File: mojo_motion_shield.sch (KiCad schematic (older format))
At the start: 1 part, among them P1 MOJO

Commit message: flesh out schematic
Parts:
- added C2, C3, C4, C5: CP_Small, Capacitors_THT:CP_Radial_D5.0mm_P2.50mm, symbol CP_Small
- added J1, J2: Conn_01x24, symbol Conn_01x24
- added J10, J11, J12, J13: Conn_01x09, symbol Conn_01x09
- added J14, J15, J16, J17, J3, J9: Conn_01x04, Pin_Headers:Pin_Header_Straight_1x04_Pitch2.54mm, symbol Conn_01x04
- added J18, J19, J5, J8: Conn_01x04, symbol Conn_01x04
- added J4: Conn_01x03, Pin_Headers:Pin_Header_Straight_1x03_Pitch2.54mm, symbol Conn_01x03
- added J6, J7: Conn_02x04_Odd_Even, Pin_Headers:Pin_Header_Straight_2x04_Pitch2.54mm, symbol Conn_02x04_Odd_Even
- added R1, R2, R3: R_Small, Resistors_THT:R_Axial_DIN0204_L3.6mm_D1.6mm_P2.54mm_Vertical, symbol R_Small
- added U2, U3, U4, U5: A4988, symbol A4988
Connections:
- net +3V3: now reaches P1.+V
- net +3V3: now also P1.+V, J4.3 (Pin_3)
- net PWM6: now reaches P1.137
- net PWM6: now also J1.7 (Pin_7)
- net PWM7: now reaches P1.138
- net PWM7: now also J1.8 (Pin_8)
- net PWM4: now reaches P1.139
- net PWM4: now also J1.5 (Pin_5)
- net PWM5: now reaches P1.140
- net PWM5: now also J1.6 (Pin_6)
- net PWM2: now reaches P1.141
- net PWM2: now also J1.3 (Pin_3)
- net PWM3: now reaches P1.142
- net PWM3: now also J1.4 (Pin_4)
- net PWM0: now reaches P1.143
- net PWM0: now also J1.1 (Pin_1)
- net PWM1: now reaches P1.144
- net PWM1: now also J1.2 (Pin_2)
- net at P1.15: now also R3.1
- net at P1.17: now also J9.3 (Pin_3)
- net at P1.22: now also R2.1
- net at P1.24: now also R1.1
- net GND: now reaches P1.GND
- net GND: now also P1.GND, P1.GND, C2.2, C3.2, C4.2, C5.2, J1.17 (Pin_17), J1.18 (Pin_18), J1.19 (Pin_19), J1.20 (Pin_20), J1.21 (Pin_21), J1.22 (Pin_22), J1.23 (Pin_23), J1.24 (Pin_24), J10.1 (Pin_1), J10.2 (Pin_2), J10.3 (Pin_3), J11.1 (Pin_1), J11.2 (Pin_2), J11.3 (Pin_3), J12.1 (Pin_1), J12.2 (Pin_2), J12.3 (Pin_3), J13.1 (Pin_1), J13.2 (Pin_2), J13.3 (Pin_3), J18.4 (Pin_4), J19.4 (Pin_4), J2.17 (Pin_17), J2.18 (Pin_18), J2.19 (Pin_19), J2.20 (Pin_20), J2.21 (Pin_21), J2.22 (Pin_22), J2.23 (Pin_23), J2.24 (Pin_24), J3.2 (Pin_2), J3.4 (Pin_4), J5.4 (Pin_4), J6.2 (Pin_2), J7.2 (Pin_2), J8.4 (Pin_4), U2.10 (GND), U2.16 (GND), U3.10 (GND), U3.16 (GND), U4.10 (GND), U4.16 (GND), U5.10 (GND), U5.16 (GND)
- net +5V: now reaches P1.RAW
- net +5V: now also P1.RAW, J4.1 (Pin_1)
- net AENCB: now reaches P1.100
- net AENCB: now also J19.3 (Pin_3)
- net ASTEP: now reaches P1.102
- net ASTEP: now also U5.7 (STEP)
- net ADIR: now reaches P1.105
- net ADIR: now also U5.8 (DIR)
- net ZSTEP: now reaches P1.112
- net ZSTEP: now also U4.7 (STEP)
- net ZDIR: now reaches P1.115
- net ZDIR: now also U4.8 (DIR)
- net CS0: now reaches P1.116
- net CS0: now also J6.3 (Pin_3)
- net MOSI: now reaches P1.117
- net MOSI: now also J6.4 (Pin_4)
- net CS1: now reaches P1.118
- net CS1: now also J6.5 (Pin_5)
- net MISO: now reaches P1.119
- net MISO: now also J6.6 (Pin_6)
- net CS2: now reaches P1.120
- net CS2: now also J6.7 (Pin_7)
- net SCK: now reaches P1.121
- net SCK: now also J6.8 (Pin_8)
- net YENCB: now reaches P1.58
- net YENCB: now also J8.3 (Pin_3)
- net YENCA: now reaches P1.67
- net YENCA: now also J8.2 (Pin_2)
- net XENCB: now reaches P1.75
- net XENCB: now also J5.3 (Pin_3)
- net XENCA: now reaches P1.79
- net XENCA: now also J5.2 (Pin_2)
- net XSTEP: now reaches P1.81
- net XSTEP: now also U2.7 (STEP)
- net XDIR: now reaches P1.83
- net XDIR: now also U2.8 (DIR)
- net YSTEP: now reaches P1.85
- net YSTEP: now also U3.7 (STEP)
- net YDIR: now reaches P1.88
- net YDIR: now also U3.8 (DIR)
- net ZENCB: now reaches P1.93
- net ZENCB: now also J18.3 (Pin_3)
- net ZENCA: now reaches P1.95
- net ZENCA: now also J18.2 (Pin_2)
- net AENCA: now reaches P1.98
- net AENCA: now also J19.2 (Pin_2)
- net A0: now reaches P1.A0
- net A0: now also J2.1 (Pin_1)
- net A1: now reaches P1.A1
- net A1: now also J2.2 (Pin_2)
- net A4: now reaches P1.A4
- net A4: now also J2.3 (Pin_3)
- net A5: now reaches P1.A5
- net A5: now also J2.4 (Pin_4)
- net A6: now reaches P1.A6
- net A6: now also J2.5 (Pin_5)
- net A7: now reaches P1.A7
- net A7: now also J2.6 (Pin_6)
- net A8: now reaches P1.A8
- net A8: now also J2.7 (Pin_7)
- net A9: now reaches P1.A9
- net A9: now also J2.8 (Pin_8)
- net AREF: now reaches P1.AREF
- net AREF: now also J2.10 (Pin_10), J2.11 (Pin_11), J2.12 (Pin_12), J2.13 (Pin_13), J2.14 (Pin_14), J2.15 (Pin_15), J2.16 (Pin_16), J2.9 (Pin_9)
- new net: J9.1 (Pin_1), R1.2
- new net: J9.2 (Pin_2), R2.2
- new net: J9.4 (Pin_4), R3.2
- new net: J14.1 (Pin_1), U2.11 (2B)
- new net: J14.2 (Pin_2), U2.12 (2A)
- new net: J14.3 (Pin_3), U2.13 (1A)
- new net: J14.4 (Pin_4), U2.14 (1B)
- new net: J10.6 (Pin_6), U2.2 (MS1)
- new net: J10.5 (Pin_5), U2.3 (MS2)
- new net: J10.4 (Pin_4), U2.4 (MS3)
- new net: U2.5 (~RST), U2.6 (~SLP)
- new net: J15.1 (Pin_1), U3.11 (2B)
- new net: J15.2 (Pin_2), U3.12 (2A)
- new net: J15.3 (Pin_3), U3.13 (1A)
- new net: J15.4 (Pin_4), U3.14 (1B)
- new net: J11.6 (Pin_6), U3.2 (MS1)
- new net: J11.5 (Pin_5), U3.3 (MS2)
- new net: J11.4 (Pin_4), U3.4 (MS3)
- new net: U3.5 (~RST), U3.6 (~SLP)
- new net: J16.1 (Pin_1), U4.11 (2B)
- new net: J16.2 (Pin_2), U4.12 (2A)
- new net: J16.3 (Pin_3), U4.13 (1A)
- new net: J16.4 (Pin_4), U4.14 (1B)
- new net: J12.6 (Pin_6), U4.2 (MS1)
- new net: J12.5 (Pin_5), U4.3 (MS2)
- new net: J12.4 (Pin_4), U4.4 (MS3)
- new net: U4.5 (~RST), U4.6 (~SLP)
- new net: J17.1 (Pin_1), U5.11 (2B)
- new net: J17.2 (Pin_2), U5.12 (2A)
- new net: J17.3 (Pin_3), U5.13 (1A)
- new net: J17.4 (Pin_4), U5.14 (1B)
- new net: J13.6 (Pin_6), U5.2 (MS1)
- new net: J13.5 (Pin_5), U5.3 (MS2)
- new net: J13.4 (Pin_4), U5.4 (MS3)
- new net: U5.5 (~RST), U5.6 (~SLP)
- new net +12V: C2.1, C3.1, C4.1, C5.1, J3.3 (Pin_3), U2.9 (VMOT), U3.9 (VMOT), U4.9 (VMOT), U5.9 (VMOT)
- new net EXTPWR: J1.10 (Pin_10), J1.11 (Pin_11), J1.12 (Pin_12), J1.13 (Pin_13), J1.14 (Pin_14), J1.15 (Pin_15), J1.16 (Pin_16), J1.9 (Pin_9), J3.1 (Pin_1)
- new net LVTTL: J10.7 (Pin_7), J10.8 (Pin_8), J10.9 (Pin_9), J11.7 (Pin_7), J11.8 (Pin_8), J11.9 (Pin_9), J12.7 (Pin_7), J12.8 (Pin_8), J12.9 (Pin_9), J13.7 (Pin_7), J13.8 (Pin_8), J13.9 (Pin_9), J18.1 (Pin_1), J19.1 (Pin_1), J4.2 (Pin_2), J5.1 (Pin_1), J6.1 (Pin_1), J7.1 (Pin_1), J8.1 (Pin_1), U2.15 (VDD), U3.15 (VDD), U4.15 (VDD), U5.15 (VDD)
- no-connect marks 14 -> 68
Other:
- moved on the sheet: P1A, P1B, P1C

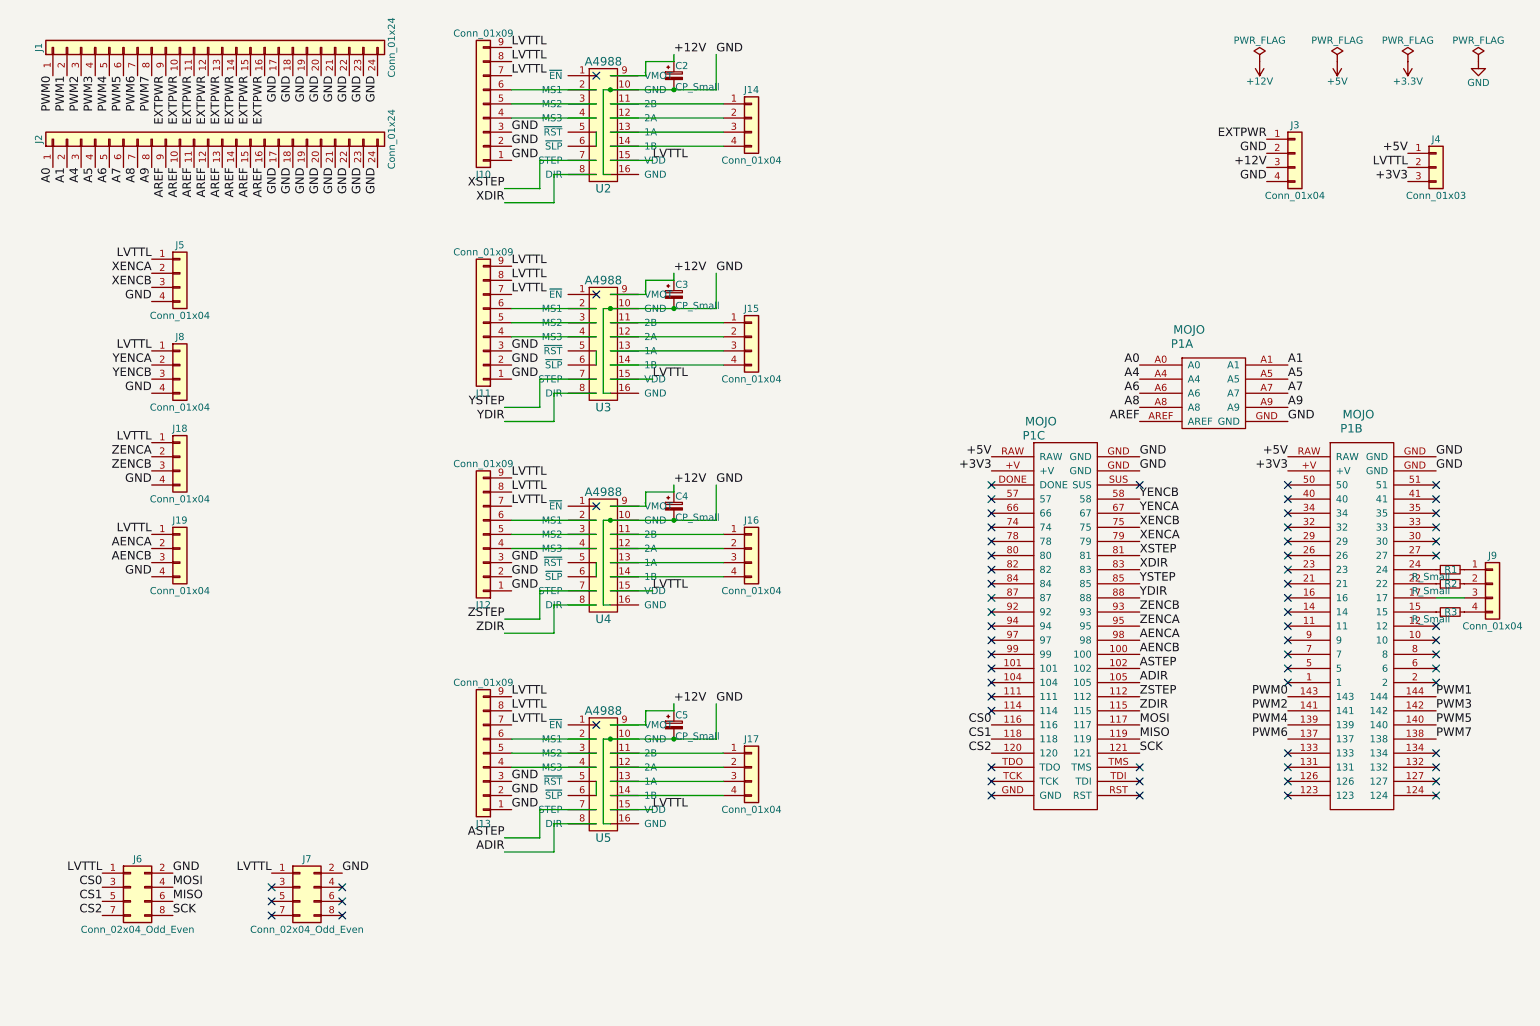
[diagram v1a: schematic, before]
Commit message: flesh out pcb layout
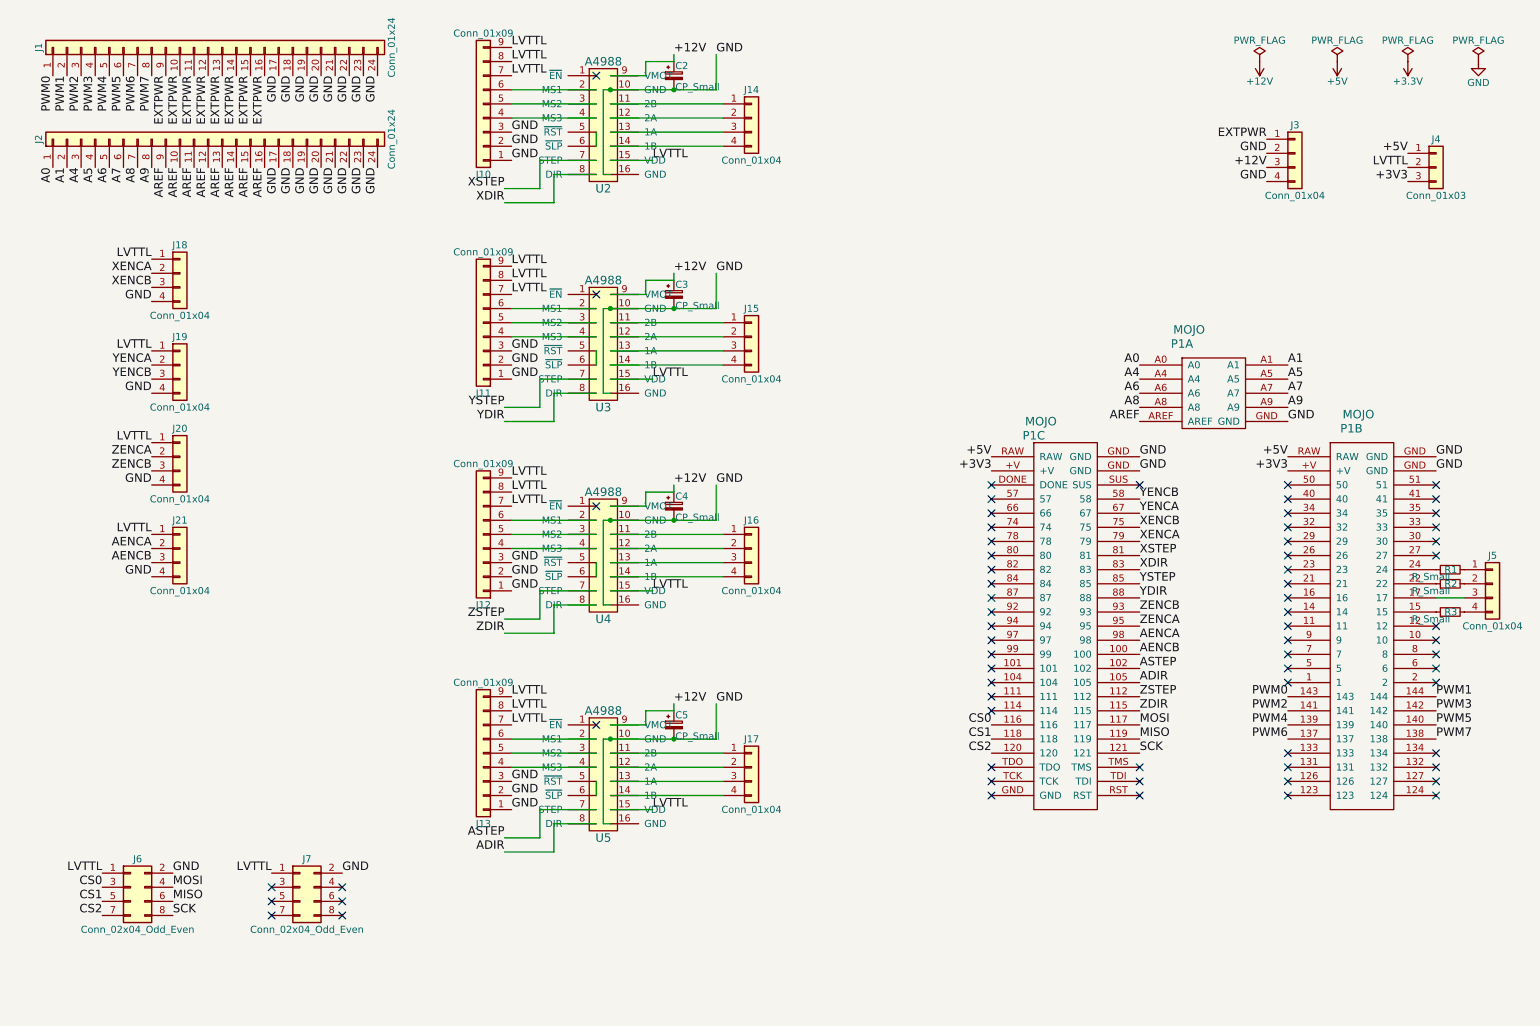
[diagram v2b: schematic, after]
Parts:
- J1, J2: footprint (none) -> mojov3:Pin_Header_Angled_3x08_Pitch2.54mm
- J10, J11, J12, J13: footprint (none) -> mojov3:Pin_Header_Straight_3x03_Pitch2.54mm
- J18: renamed from J5; footprint (none) -> Pin_Headers:Pin_Header_Straight_1x04_Pitch2.54mm
- J19: renamed from J8; footprint (none) -> Pin_Headers:Pin_Header_Straight_1x04_Pitch2.54mm
- J20: renamed from J18; footprint (none) -> Pin_Headers:Pin_Header_Straight_1x04_Pitch2.54mm
- J21: renamed from J19; footprint (none) -> Pin_Headers:Pin_Header_Straight_1x04_Pitch2.54mm
- U2, U3, U4, U5: footprint (none) -> mojov3:A4988
- renumbered J9 to J5
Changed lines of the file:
@@
 F 0 "J2" H 1850 2700 50  0000 C CNN
 F 1 "Conn_01x24" H 1850 200 50  0000 C CNN
-F 2 "" H 1850 1500 50  0001 C CNN
+F 2 "mojov3:Pin_Header_Angled_3x08_Pitch2.54mm" H 1850 1500 50  0001 C CNN
 F 3 "" H 1850 1500 50  0001 C CNN
 	1    1850 1500
@@
 F 0 "J1" H 1850 2050 50  0000 C CNN
 F 1 "Conn_01x24" H 1850 -450 50  0000 C CNN
-F 2 "" H 1850 850 50  0001 C CNN
+F 2 "mojov3:Pin_Header_Angled_3x08_Pitch2.54mm" H 1850 850 50  0001 C CNN
 F 3 "" H 1850 850 50  0001 C CNN
 	1    1850 850
@@
 $EndComp
 $Comp
-L Conn_01x04 J9
+L Conn_01x04 J5
 U 1 1 5A459FF1
 P 10950 4650
-F 0 "J9" H 10950 4850 50  0000 C CNN
+F 0 "J5" H 10950 4850 50  0000 C CNN
 F 1 "Conn_01x04" H 10950 4350 50  0000 C CNN
 F 2 "Pin_Headers:Pin_Header_Straight_1x04_Pitch2.54mm" H 10950 4650 50  0001 C CNN
@@
 F 0 "U2" H 4650 650 60  0000 C CNN
 F 1 "A4988" H 4650 1550 60  0000 C CNN
-F 2 "" H 4650 1250 60  0001 C CNN
+F 2 "mojov3:A4988" H 4650 1250 60  0001 C CNN
 F 3 "" H 4650 1250 60  0001 C CNN
 	1    4650 1250
@@
 F 0 "J10" H 3800 1750 50  0000 C CNN
 F 1 "Conn_01x09" H 3800 750 50  0000 C CNN
-F 2 "" H 3800 1250 50  0001 C CNN
+F 2 "mojov3:Pin_Header_Straight_3x03_Pitch2.54mm" H 3800 1250 50  0001 C CNN
 F 3 "" H 3800 1250 50  0001 C CNN
 	1    3800 1250
@@
 F 0 "U3" H 4650 2200 60  0000 C CNN
 F 1 "A4988" H 4650 3100 60  0000 C CNN
-F 2 "" H 4650 2800 60  0001 C CNN
+F 2 "mojov3:A4988" H 4650 2800 60  0001 C CNN
 F 3 "" H 4650 2800 60  0001 C CNN
 	1    4650 2800
@@
 F 0 "J11" H 3800 3300 50  0000 C CNN
 F 1 "Conn_01x09" H 3800 2300 50  0000 C CNN
-F 2 "" H 3800 2800 50  0001 C CNN
+F 2 "mojov3:Pin_Header_Straight_3x03_Pitch2.54mm" H 3800 2800 50  0001 C CNN
 F 3 "" H 3800 2800 50  0001 C CNN
 	1    3800 2800
@@
 F 0 "U4" H 4650 3700 60  0000 C CNN
 F 1 "A4988" H 4650 4600 60  0000 C CNN
-F 2 "" H 4650 4300 60  0001 C CNN
+F 2 "mojov3:A4988" H 4650 4300 60  0001 C CNN
 F 3 "" H 4650 4300 60  0001 C CNN
 	1    4650 4300
@@
 F 0 "J12" H 3800 4800 50  0000 C CNN
 F 1 "Conn_01x09" H 3800 3800 50  0000 C CNN
-F 2 "" H 3800 4300 50  0001 C CNN
+F 2 "mojov3:Pin_Header_Straight_3x03_Pitch2.54mm" H 3800 4300 50  0001 C CNN
 F 3 "" H 3800 4300 50  0001 C CNN
 	1    3800 4300
@@
 F 0 "U5" H 4650 5250 60  0000 C CNN
 F 1 "A4988" H 4650 6150 60  0000 C CNN
-F 2 "" H 4650 5850 60  0001 C CNN
+F 2 "mojov3:A4988" H 4650 5850 60  0001 C CNN
 F 3 "" H 4650 5850 60  0001 C CNN
 	1    4650 5850
@@
 F 0 "J13" H 3800 6350 50  0000 C CNN
 F 1 "Conn_01x09" H 3800 5350 50  0000 C CNN
-F 2 "" H 3800 5850 50  0001 C CNN
+F 2 "mojov3:Pin_Header_Straight_3x03_Pitch2.54mm" H 3800 5850 50  0001 C CNN
 F 3 "" H 3800 5850 50  0001 C CNN
 	1    3800 5850
@@
 NoConn ~ 2800 7000
 $Comp
-L Conn_01x04 J5
+L Conn_01x04 J18
 U 1 1 5A45E354
 P 1650 2450
-F 0 "J5" H 1650 2650 50  0000 C CNN
+F 0 "J18" H 1650 2650 50  0000 C CNN
 F 1 "Conn_01x04" H 1650 2150 50  0000 C CNN
-F 2 "" H 1650 2450 50  0001 C CNN
+F 2 "Pin_Headers:Pin_Header_Straight_1x04_Pitch2.54mm" H 1650 2450 50  0001 C CNN
 F 3 "" H 1650 2450 50  0001 C CNN
 	1    1650 2450
@@
 $EndComp
 $Comp
-L Conn_01x04 J8
+L Conn_01x04 J19
 U 1 1 5A45E421
 P 1650 3100
-F 0 "J8" H 1650 3300 50  0000 C CNN
+F 0 "J19" H 1650 3300 50  0000 C CNN
 F 1 "Conn_01x04" H 1650 2800 50  0000 C CNN
-F 2 "" H 1650 3100 50  0001 C CNN
+F 2 "Pin_Headers:Pin_Header_Straight_1x04_Pitch2.54mm" H 1650 3100 50  0001 C CNN
 F 3 "" H 1650 3100 50  0001 C CNN
 	1    1650 3100
@@
 $EndComp
 $Comp
-L Conn_01x04 J18
+L Conn_01x04 J20
 U 1 1 5A45E549
 P 1650 3750
-F 0 "J18" H 1650 3950 50  0000 C CNN
+F 0 "J20" H 1650 3950 50  0000 C CNN
 F 1 "Conn_01x04" H 1650 3450 50  0000 C CNN
-F 2 "" H 1650 3750 50  0001 C CNN
+F 2 "Pin_Headers:Pin_Header_Straight_1x04_Pitch2.54mm" H 1650 3750 50  0001 C CNN
 F 3 "" H 1650 3750 50  0001 C CNN
 	1    1650 3750
@@
 $EndComp
 $Comp
-L Conn_01x04 J19
+L Conn_01x04 J21
 U 1 1 5A45E657
 P 1650 4400
-F 0 "J19" H 1650 4600 50  0000 C CNN
+F 0 "J21" H 1650 4600 50  0000 C CNN
 F 1 "Conn_01x04" H 1650 4100 50  0000 C CNN
-F 2 "" H 1650 4400 50  0001 C CNN
+F 2 "Pin_Headers:Pin_Header_Straight_1x04_Pitch2.54mm" H 1650 4400 50  0001 C CNN
 F 3 "" H 1650 4400 50  0001 C CNN
 	1    1650 4400
